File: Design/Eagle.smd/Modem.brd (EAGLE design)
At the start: 26.3 x 24.1 mm, 23 parts, among them Q1 BSS123

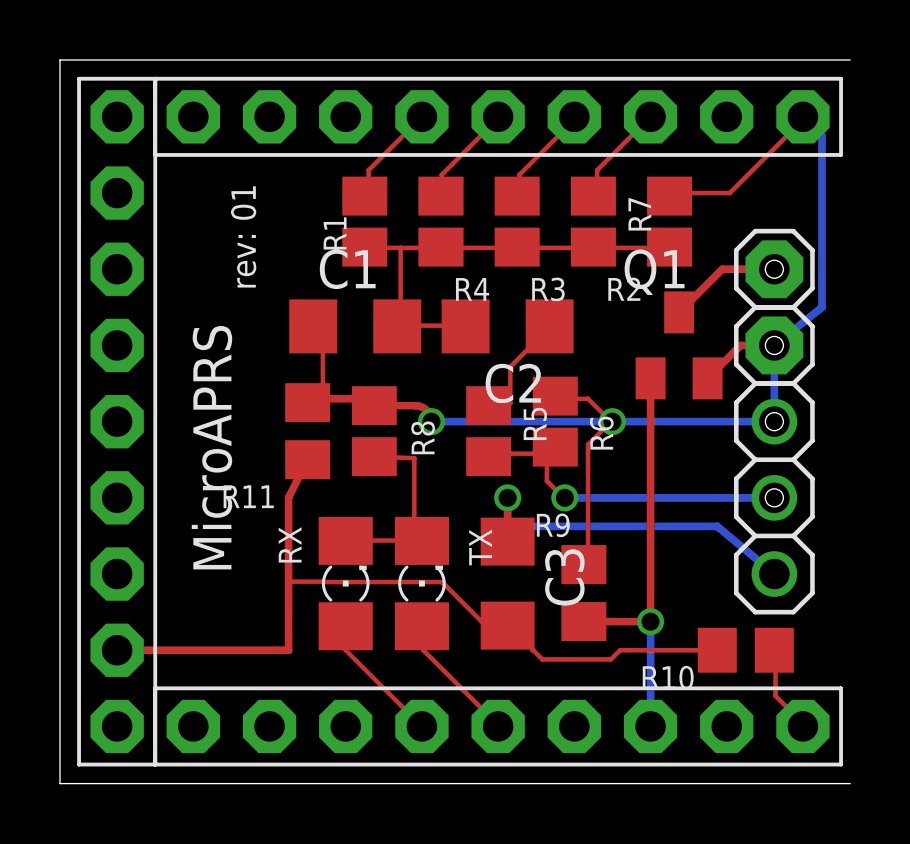
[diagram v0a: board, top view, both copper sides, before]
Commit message: Add input filter
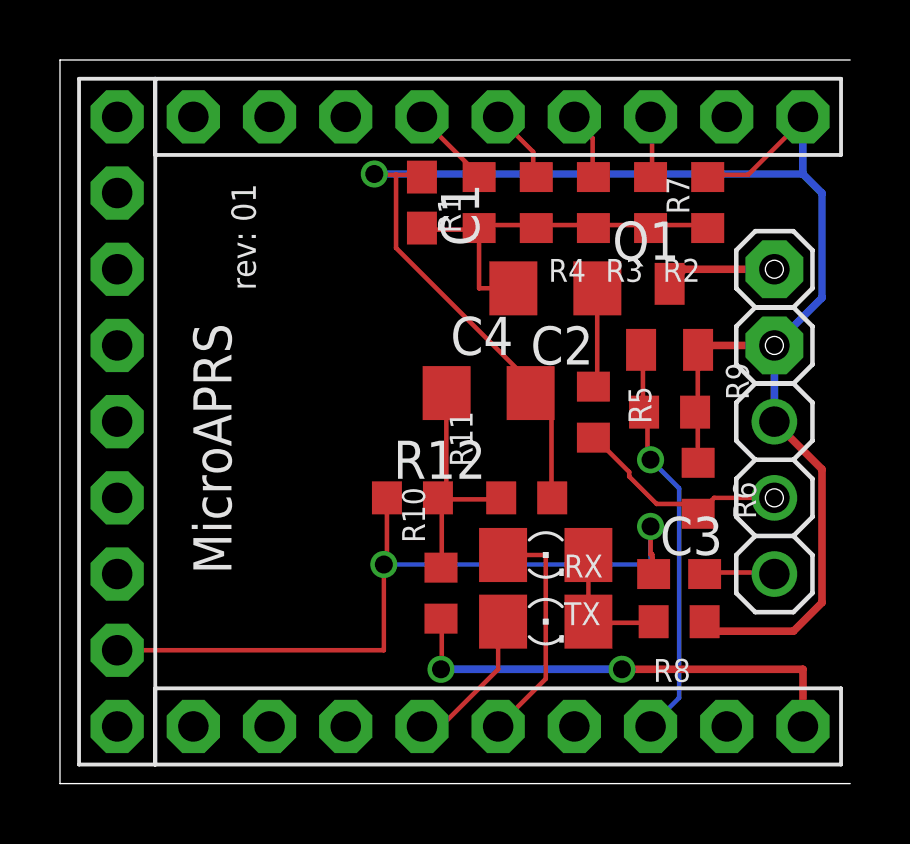
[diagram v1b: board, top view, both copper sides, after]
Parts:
- added C4: 10uf, rcl:C1206
- added R12: 10k, rcl:R0603
- C1: device eagle-ltspice:C1206 -> eagle-ltspice:C0603
- C3: value 1uf -> 220nf; device eagle-ltspice:C1206 -> rcl:C0603
- R1, R2, R3, R4, R5, R6, R7, R8: device resistor:R0805 -> resistor:R0603
- R10, R11: value 100k -> 10k; device rcl:R0805 -> rcl:R0603
- R9: device rcl:R0805 -> rcl:R0603
- moved R8 12.0 mm to (37.8, 54.3), turned to 0 degrees
- moved R10 10.3 mm to (29.8, 55.2), turned to 90 degrees
- moved R11 7.63 mm to (32.7, 58.4), turned to 180 degrees
- moved RX 6.79 mm to (33.3, 54.3), turned to 0 degrees
- moved R9 6.68 mm to (37.5, 61.3), turned to 0 degrees
- moved C3 5.72 mm to (37.8, 55.9), turned to 0 degrees
- moved R6 5.26 mm to (38.4, 58.7)
- moved C1 4.69 mm to (29.2, 68.3), turned to 270 degrees
- moved TX 4.24 mm to (33.3, 56.5), turned to 0 degrees
- moved R1 3.86 mm to (31.1, 68.3)
- moved R5 3.55 mm to (34.9, 61.3)
- moved R4 3.24 mm to (33.0, 68.3)
- moved R3 2.62 mm to (34.9, 68.3)
- moved C2 2.03 mm to (33.7, 65.4)
- moved R2 2.01 mm to (36.8, 68.3)
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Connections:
- new net N$10: C4.1, R10.2, R11.2, R12.2
- net A0: now also C3.1, R12.1; no longer C3.2, R10.2, R11.2
- net GND: now also C4.2
- net LINE_LEVEL_IN: now also C3.2; no longer C3.1
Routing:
- net GND: track 46.3 -> 62.4 mm, vias 2 -> 1
- net 5V: track 2.96 -> 15.7 mm, vias 0 -> 2
- net LINE_LEVEL_IN: track 12.2 -> 2.35 mm, vias 1 -> 0
- net N$10: track 0.00 -> 8.28 mm
- net MIC_LEVEL_OUT: track 11.5 -> 7.39 mm, vias 1 -> 0
- net D9: track 4.39 -> 7.79 mm
- net A0: track 29.2 -> 26.5 mm, vias 0 -> 2
- net N$1: track 6.69 -> 4.41 mm
- net N$5: track 15.1 -> 13.5 mm
- net D6: track 3.44 -> 2.03 mm
- net D5: track 3.43 -> 2.26 mm
- net D4: track 3.42 -> 2.54 mm
- net D3: track 3.44 -> 2.78 mm
- net D10: track 4.39 -> 4.99 mm
- net D7: track 14.3 -> 13.8 mm
